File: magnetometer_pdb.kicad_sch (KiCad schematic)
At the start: 61 parts, among them J1 Screw_Terminal_01x02, J10 Screw_Terminal_01x02, J11 Screw_Terminal_01x02, J12 Screw_Terminal_01x02, J13 Screw_Terminal_01x02, J14 Screw_Terminal_01x02, J2 Screw_Terminal_01x02, J3 Screw_Terminal_01x02, J4 Screw_Terminal_01x02, J5 Screw_Terminal_01x02, J6 Conn_01x02_Pin, J7 Conn_01x02_Pin, J8 Conn_01x02_Pin, J9 Screw_Terminal_01x02, U1 TPS56528DDA, U2 L78L09_SO8, U3 ${SIM.PARAMS}, U4 ${SIM.PARAMS}, U5 ${SIM.PARAMS}, U6 ${SIM.PARAMS}

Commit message: Modified schematic and pcb
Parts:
- removed C1: 0.1u, Capacitor_SMD:C_0805_2012Metric_Pad1.18x1.45mm_HandSolder, symbol Device:C_Small
- removed C3, C4: 10u, Capacitor_SMD:C_0805_2012Metric_Pad1.18x1.45mm_HandSolder, symbol Device:C
- removed C6, C7: 22u, Capacitor_SMD:C_0805_2012Metric_Pad1.18x1.45mm_HandSolder, symbol Device:C_Small
- removed C8: .47u, Capacitor_SMD:C_0805_2012Metric_Pad1.18x1.45mm_HandSolder, symbol Device:C_Small
- removed J5: Screw_Terminal_01x02, Connector_PinHeader_2.00mm:2_Pin_Screw_Term, symbol Connector:Screw_Terminal_01x02
- removed L1: 1.5u, Inductor_SMD:SPM6530T-1R5M100, symbol Device:L_Iron
- removed R1: 10k, Resistor_SMD:R_0805_2012Metric_Pad1.20x1.40mm_HandSolder, symbol Device:R_US
- removed R2: 365k, Resistor_SMD:R_0805_2012Metric_Pad1.20x1.40mm_HandSolder, symbol Device:R_US
- removed R3: 100k, Resistor_SMD:R_0805_2012Metric_Pad1.20x1.40mm_HandSolder, symbol Device:R_US
- removed R5: 49.9k, Resistor_SMD:R_0805_2012Metric_Pad1.20x1.40mm_HandSolder, symbol Device:R_US
- removed U1: TPS56528DDA, Package_SO:Texas_HSOP-8-1EP_3.9x4.9mm_P1.27mm_ThermalVias, symbol Regulator_Switching:TPS56528DDA
- added C11, C24: 10u, Capacitor_SMD:C_0805_2012Metric_Pad1.18x1.45mm_HandSolder, symbol Device:C_Small
- added C25: 2.2u, Capacitor_SMD:C_0805_2012Metric_Pad1.18x1.45mm_HandSolder, symbol Device:C_Small
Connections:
- net 9V_out: now also C11.1, C25.1
- net Bat_GND: now also C11.2, C24.2, C25.2
- net GND: now also U3.2 (-); no longer U3.3 (+)
- net Vin: now also C24.1
- net at C2.1, R4.2, R6.1: now also U3.3 (+); no longer U3.2 (-)
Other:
- added sheet 5v Power Supply (5v Power Supply.kicad_sch)
- note removed: "Battery Negative Terminal GND (Bat_GND)"

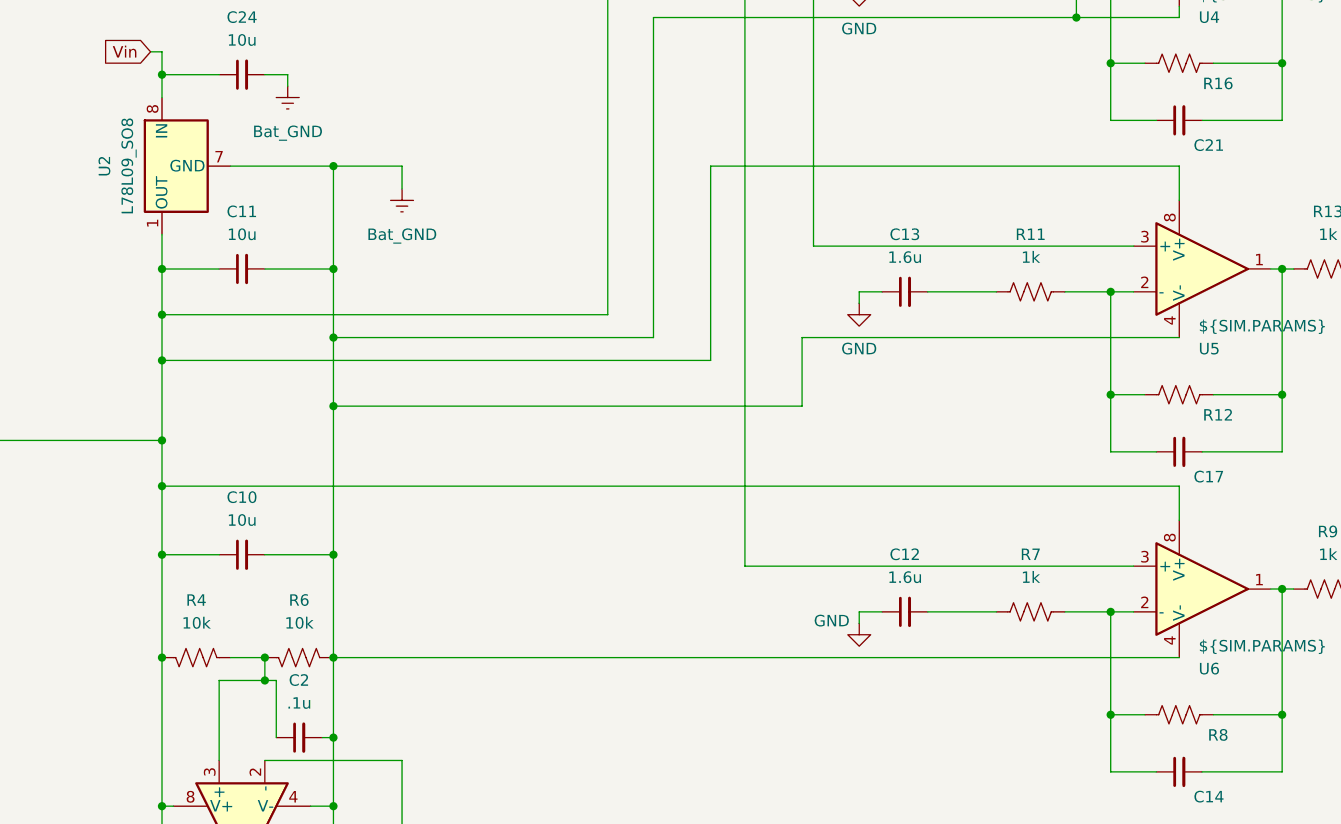
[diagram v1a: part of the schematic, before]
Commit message: Added decoupling caps
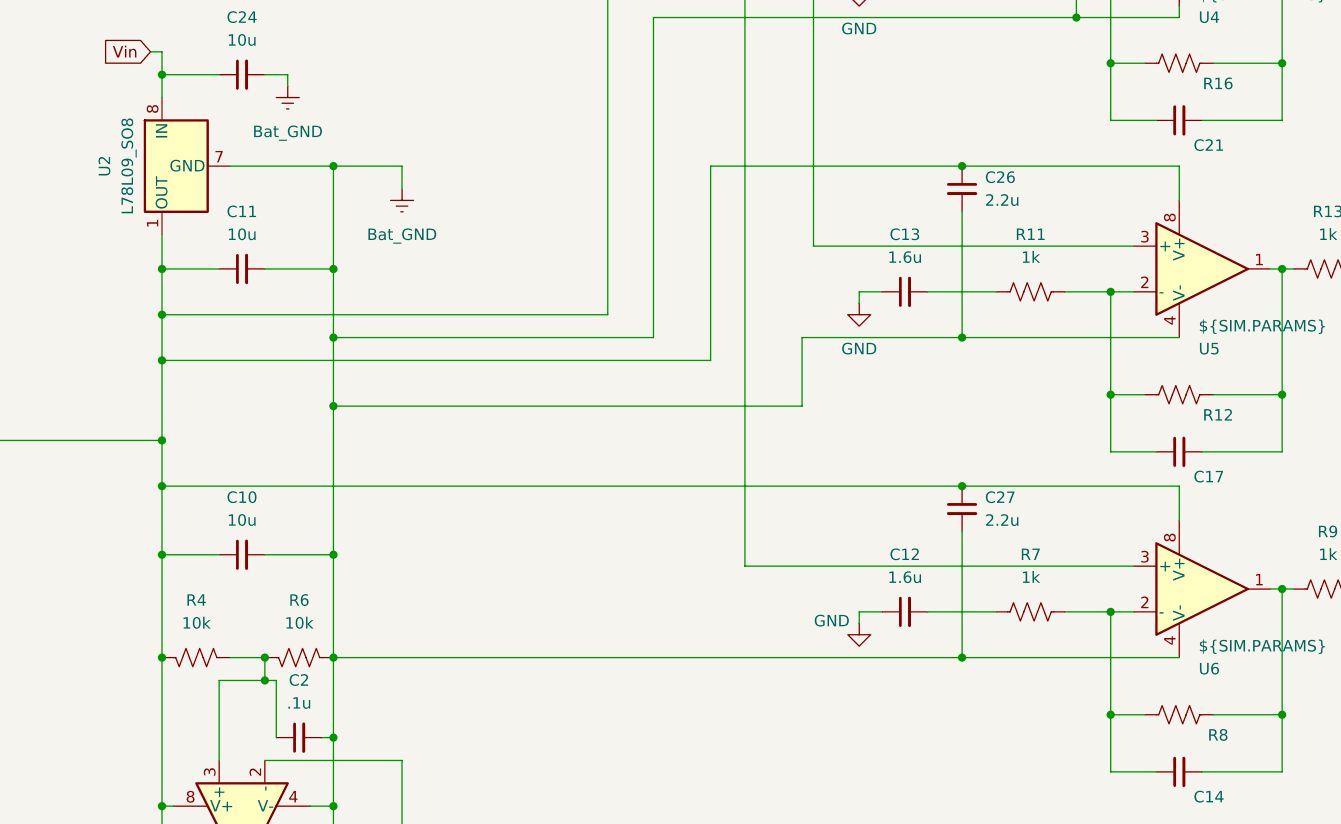
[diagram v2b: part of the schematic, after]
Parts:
- added C26, C27: 2.2u, Capacitor_SMD:C_0805_2012Metric_Pad1.18x1.45mm_HandSolder, symbol Device:C_Small
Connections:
- net 9V_out: now also C26.1, C27.1
- net Bat_GND: now also C26.2, C27.2
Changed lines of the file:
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@@
 	)
 	(junction
+		(at 190.5 83.82)
+		(diameter 0)
+		(color 0 0 0 0)
+	)
+	(junction
 		(at 33.02 92.71)
 		(diameter 0)
@@
 	)
 	(junction
+		(at 190.5 138.43)
+		(diameter 0)
+		(color 0 0 0 0)
+	)
+	(junction
 		(at 203.2 67.31)
 		(diameter 0)
@@
 	)
 	(junction
+		(at 190.5 119.38)
+		(diameter 0)
+		(color 0 0 0 0)
+	)
+	(junction
 		(at 101.6 154.94)
 		(diameter 0)
@@
 	)
 	(junction
+		(at 190.5 102.87)
+		(diameter 0)
+		(color 0 0 0 0)
+	)
+	(junction
 		(at 39.37 120.65)
 		(diameter 0)
@@
 	(wire
 		(pts
-			(xy 214.63 83.82) (xy 162.56 83.82)
+			(xy 214.63 83.82) (xy 190.5 83.82)
 		)
 		(stroke
@@
 	(wire
 		(pts
-			(xy 120.65 138.43) (xy 214.63 138.43)
+			(xy 120.65 138.43) (xy 190.5 138.43)
 		)
 		(stroke
@@
 	(wire
 		(pts
-			(xy 101.6 119.38) (xy 214.63 119.38)
+			(xy 101.6 119.38) (xy 190.5 119.38)
 		)
 		(stroke
@@
 	(wire
 		(pts
+			(xy 190.5 102.87) (xy 172.72 102.87)
+		)
+		(stroke
+			(width 0)
+			(type default)
+		)
+	)
+	(wire
+		(pts
 			(xy 33.02 71.12) (xy 33.02 92.71)
 		)
@@
 	(wire
 		(pts
+			(xy 190.5 88.9) (xy 190.5 102.87)
+		)
+		(stroke
+			(width 0)
+			(type default)
+		)
+	)
+	(wire
+		(pts
 			(xy 120.65 83.82) (xy 128.27 83.82)
 		)
@@
 	(wire
 		(pts
+			(xy 190.5 138.43) (xy 214.63 138.43)
+		)
+		(stroke
+			(width 0)
+			(type default)
+		)
+	)
+	(wire
+		(pts
 			(xy 39.37 127) (xy 39.37 134.62)
 		)
@@
 	(wire
 		(pts
+			(xy 190.5 119.38) (xy 214.63 119.38)
+		)
+		(stroke
+			(width 0)
+			(type default)
+		)
+	)
+	(wire
+		(pts
+			(xy 190.5 83.82) (xy 162.56 83.82)
+		)
+		(stroke
+			(width 0)
+			(type default)
+		)
+	)
+	(wire
+		(pts
 			(xy 107.95 140.97) (xy 107.95 149.86)
 		)
@@
 	(wire
 		(pts
-			(xy 214.63 102.87) (xy 172.72 102.87)
+			(xy 214.63 102.87) (xy 190.5 102.87)
 		)
 		(stroke
@@
 	(wire
 		(pts
+			(xy 190.5 124.46) (xy 190.5 138.43)
+		)
+		(stroke
+			(width 0)
+			(type default)
+		)
+	)
+	(wire
+		(pts
 			(xy 114.3 140.97) (xy 114.3 147.32)
 		)
@@
 	(symbol
 		(lib_id "Device:C_Small")
+		(at 190.5 121.92 0)
+		(unit 1)
+		(exclude_from_sim no)
+		(in_bom yes)
+		(on_board yes)
+		(dnp no)
+		(fields_autoplaced yes)
+		(property "Reference" "C27"
+			(at 193.04 120.6562 0)
+			(effects
+				(font
+					(size 1.27 1.27)
+				)
+				(justify left)
+			)
+		)
+		(property "Value" "2.2u"
+			(at 193.04 123.1962 0)
+			(effects
+				(font
+					(size 1.27 1.27)
+				)
+				(justify left)
+			)
+		)
+		(property "Footprint" "Capacitor_SMD:C_0805_2012Metric_Pad1.18x1.45mm_HandSolder"
+			(at 190.5 121.92 0)
+			(effects
+				(font
+					(size 1.27 1.27)
+				)
+				(hide yes)
+			)
+		)
+		(property "Datasheet" "~"
+			(at 190.5 121.92 0)
+			(effects
+				(font
+					(size 1.27 1.27)
+				)
+				(hide yes)
+			)
+		)
+		(property "Description" "Unpolarized capacitor, small symbol"
+			(at 190.5 121.92 0)
+			(effects
+				(font
+					(size 1.27 1.27)
+				)
+				(hide yes)
+			)
+		)
+		(pin "1"
+		)
+		(pin "2"
+		)
+		(instances
+			(project "magnetometer_pdb"
+				(path "/bc0e619f-307e-4ebe-8a52-967fc0be98ce"
+					(reference "C27")
+					(unit 1)
+				)
+			)
+		)
+	)
+	(symbol
+		(lib_id "Device:C_Small")
 		(at 236.22 62.23 0)
 		(unit 1)
@@
 					(unit 1)
 				)
+			)
+		)
+	)
+	(symbol
+		(lib_id "Device:C_Small")
+		(at 190.5 86.36 0)
+		(unit 1)
+		(exclude_from_sim no)
+		(in_bom yes)
+		(on_board yes)
+		(dnp no)
+		(fields_autoplaced yes)
+		(property "Reference" "C26"
+			(at 193.04 85.0962 0)
+			(effects
+				(font
+					(size 1.27 1.27)
+				)
+				(justify left)
+			)
+		)
+		(property "Value" "2.2u"
+			(at 193.04 87.6362 0)
+			(effects
+				(font
+					(size 1.27 1.27)
+				)
+				(justify left)
+			)
+		)
+		(property "Footprint" "Capacitor_SMD:C_0805_2012Metric_Pad1.18x1.45mm_HandSolder"
+			(at 190.5 86.36 0)
+			(effects
+				(font
+					(size 1.27 1.27)
+				)
+				(hide yes)
+			)
+		)
+		(property "Datasheet" "~"
+			(at 190.5 86.36 0)
+			(effects
+				(font
+					(size 1.27 1.27)
+				)
+				(hide yes)
+			)
+		)
+		(property "Description" "Unpolarized capacitor, small symbol"
+			(at 190.5 86.36 0)
+			(effects
+				(font
+					(size 1.27 1.27)
+				)
+				(hide yes)
+			)
+		)
+		(pin "1"
+		)
+		(pin "2"
+		)
+		(instances
+			(project "magnetometer_pdb"
+				(path "/bc0e619f-307e-4ebe-8a52-967fc0be98ce"
+					(reference "C26")
+					(unit 1)
+				)
